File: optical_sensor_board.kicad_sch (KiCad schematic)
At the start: 33 parts, among them J2 Conn_01x09_Socket, U1 PMW3389DM‐T3QU, U3 LM317L_SOT-89

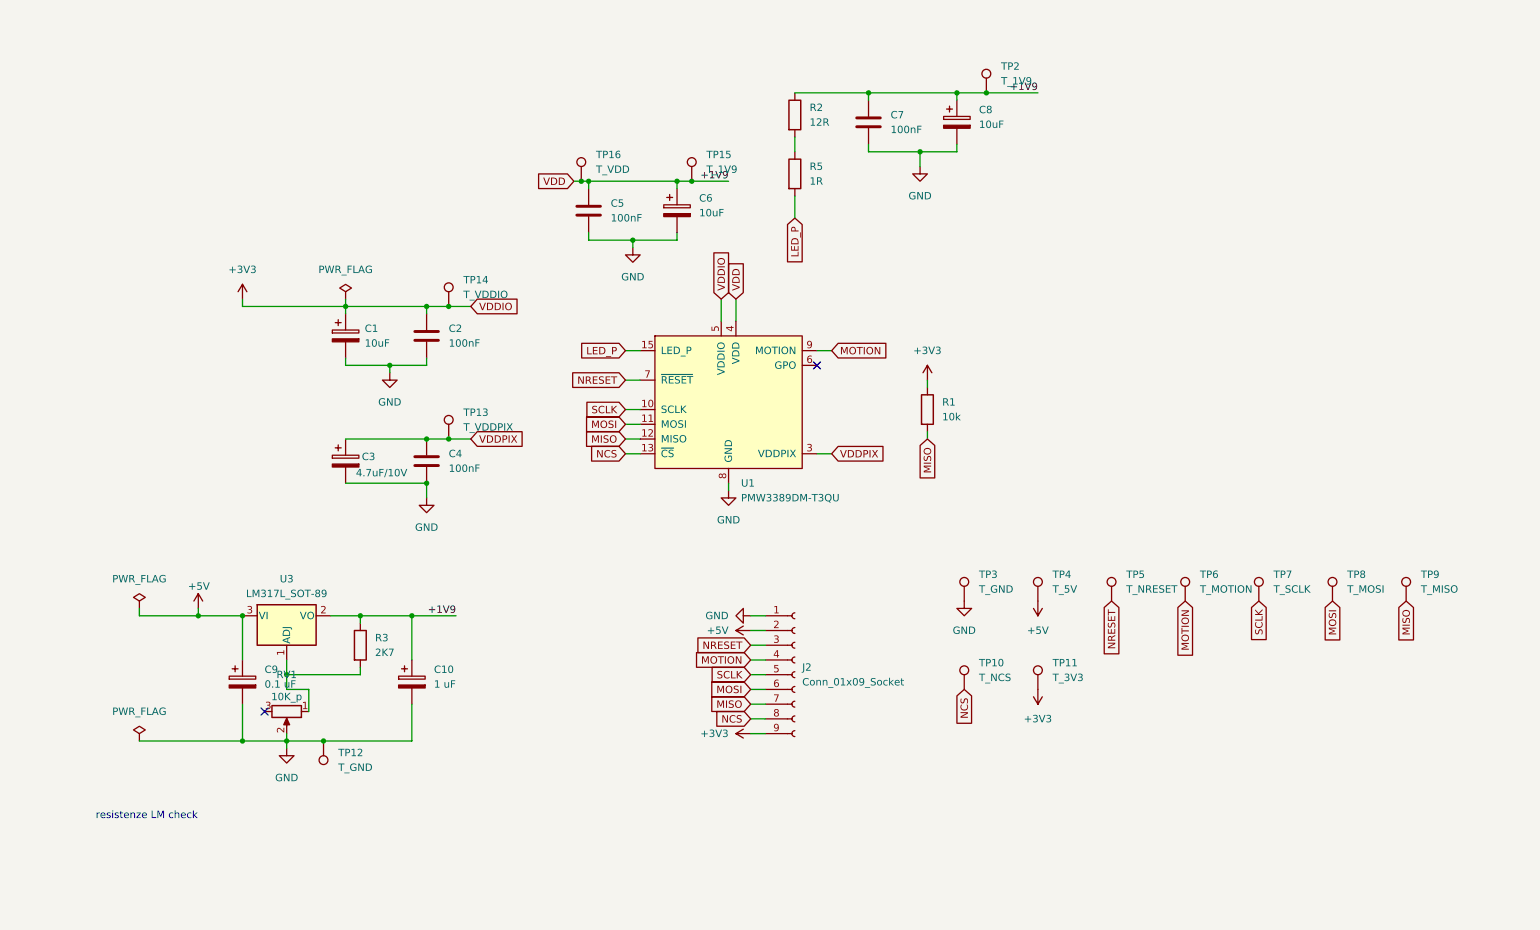
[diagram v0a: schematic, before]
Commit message: Modificato graficamente lo schematico + moidifiche al PCB
 - Sistemato graficamente lo schema
 - Corretto il testo del PCB
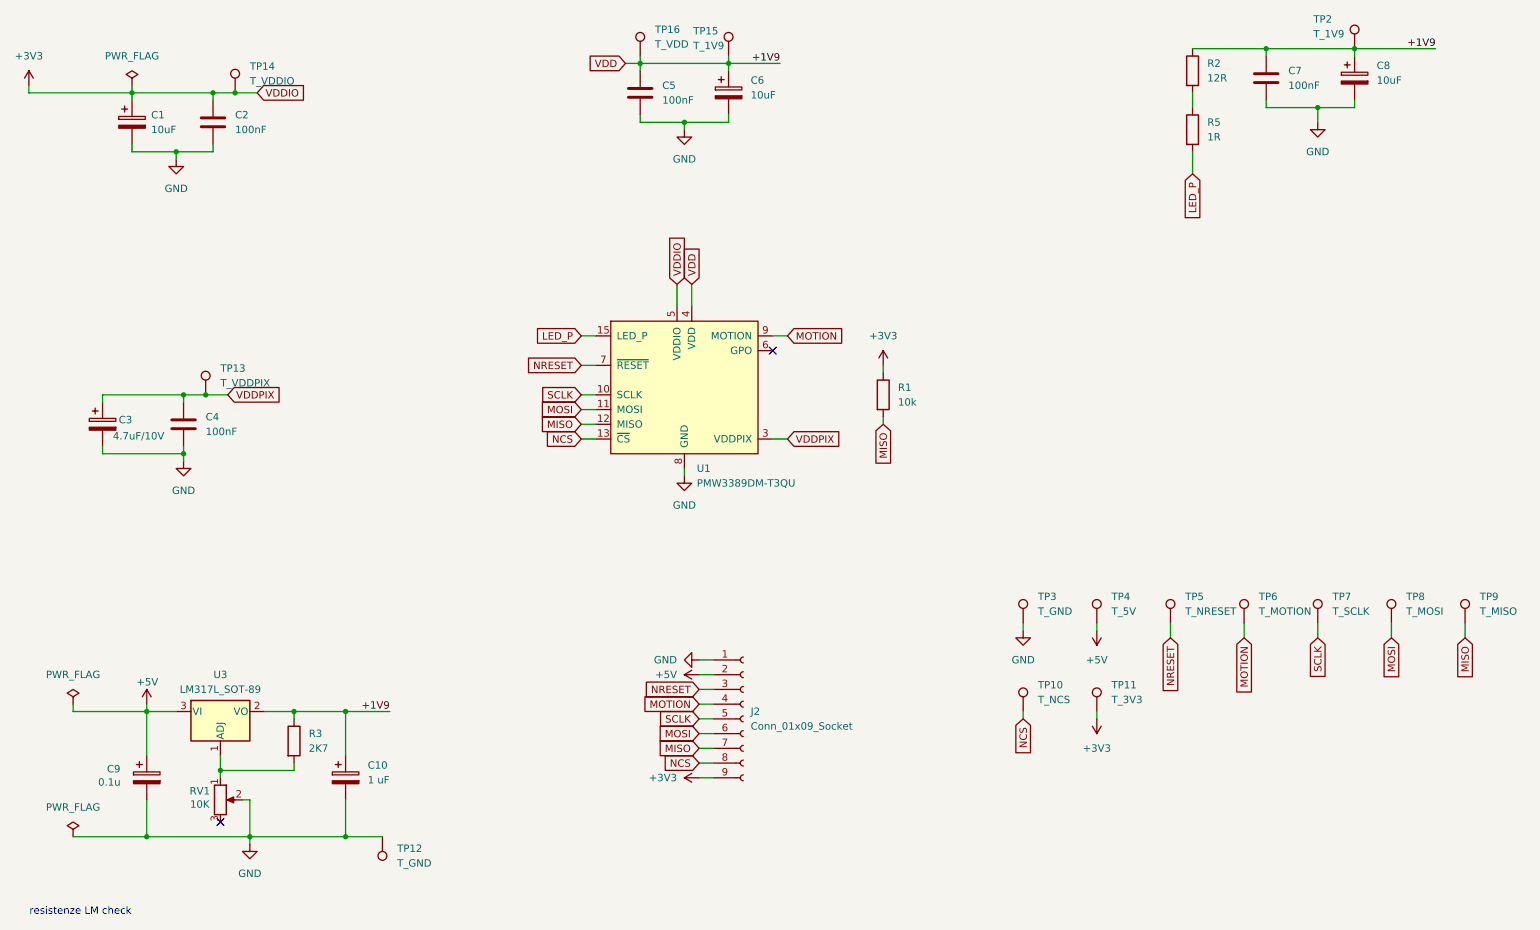
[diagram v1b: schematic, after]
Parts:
- C9: value 0.1 uF -> 0.1u
- RV1: value 10K_p -> 10K
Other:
- moved on the sheet: C1, C10, C2, C3, C4, C5, C6, C7, C8, C9, J2, R1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

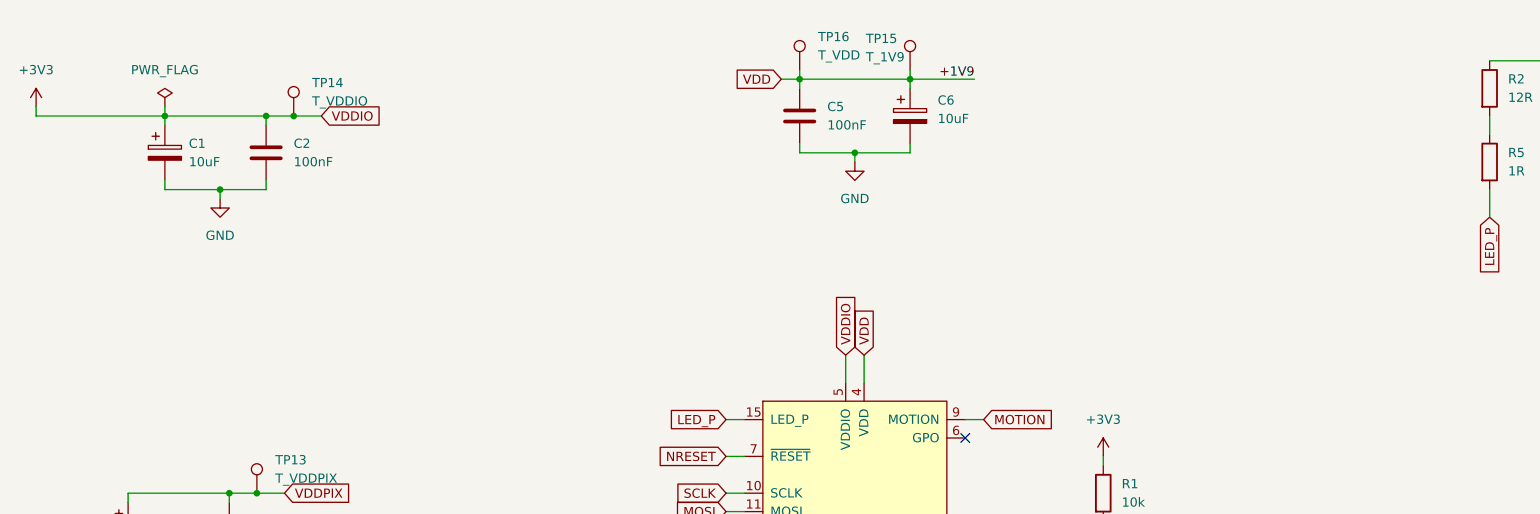
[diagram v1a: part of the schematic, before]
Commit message: Added a solder-jumer in series to the PS of the chip
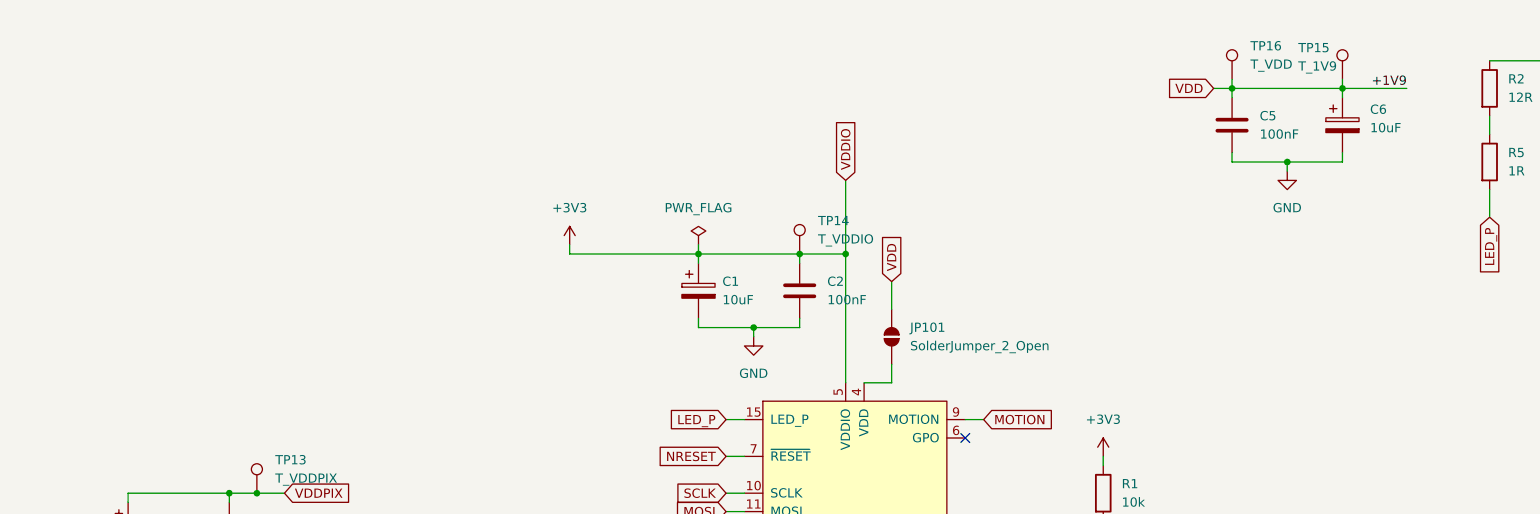
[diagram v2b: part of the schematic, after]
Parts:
- added JP101: SolderJumper_2_Open, Jumper:SolderJumper-2_P1.3mm_Open_TrianglePad1.0x1.5mm, symbol Jumper:SolderJumper_2_Open
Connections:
- net VDD: now also JP101.1 (A); no longer U1.4 (VDD)
- new net: JP101.2 (B), U1.4 (VDD)
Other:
- moved on the sheet: C1, C2, C5, C6, TP14, TP15, TP16

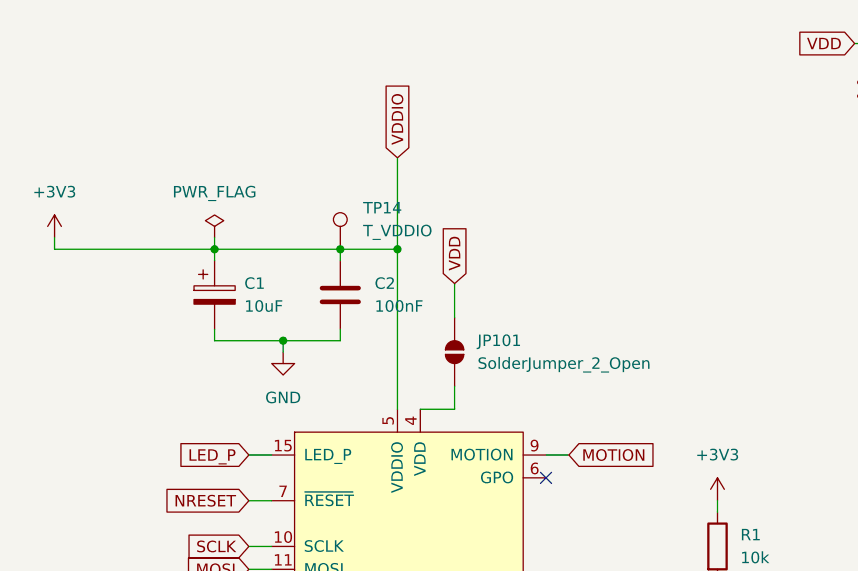
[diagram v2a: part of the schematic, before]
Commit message: Modified some traks of the PCB + exported new PDF for mastering
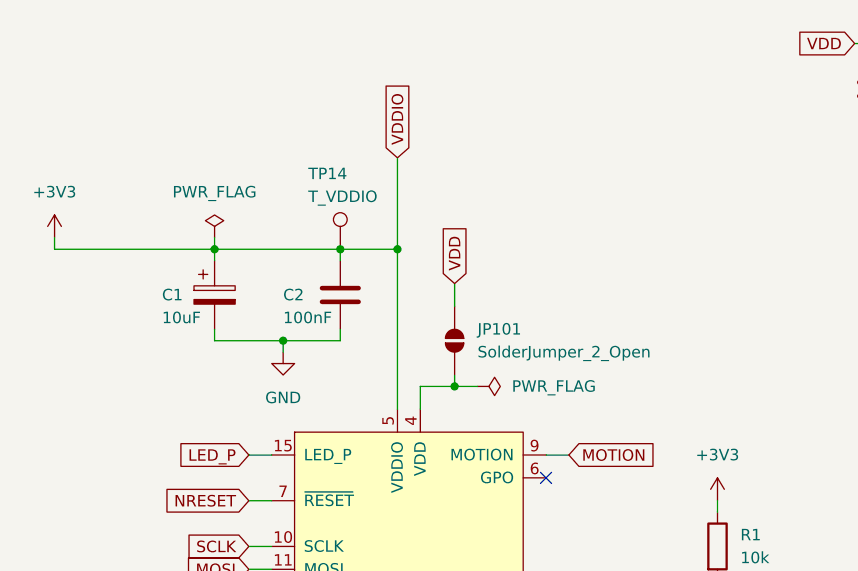
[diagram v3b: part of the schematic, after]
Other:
- moved on the sheet: JP101
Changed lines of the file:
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@@
 	)
 	(junction
+		(at 142.24 76.2)
+		(diameter 0)
+		(color 0 0 0 0)
+	)
+	(junction
 		(at 189.23 38.1)
 		(diameter 0)
@@
 	(wire
 		(pts
+			(xy 138.43 76.2) (xy 142.24 76.2)
+		)
+		(stroke
+			(width 0)
+			(type default)
+		)
+	)
+	(wire
+		(pts
 			(xy 50.8 95.25) (xy 50.8 93.98)
 		)
@@
 	(wire
 		(pts
-			(xy 142.24 64.77) (xy 142.24 68.58)
+			(xy 142.24 64.77) (xy 142.24 67.31)
 		)
 		(stroke
@@
 	(wire
 		(pts
-			(xy 142.24 78.74) (xy 138.43 78.74)
+			(xy 142.24 76.2) (xy 142.24 74.93)
 		)
 		(stroke
@@
 	(wire
 		(pts
-			(xy 142.24 76.2) (xy 142.24 78.74)
+			(xy 138.43 76.2) (xy 138.43 78.74)
 		)
 		(stroke
@@
 		)
 	)
+	(wire
+		(pts
+			(xy 144.78 76.2) (xy 142.24 76.2)
+		)
+		(stroke
+			(width 0)
+			(type default)
+		)
+	)
 	(label "+1V9"
 		(at 266.7 34.29 180)
@@
 		(on_board yes)
 		(dnp no)
-		(fields_autoplaced yes)
 		(property "Reference" "TP14"
-			(at 132.08 56.3879 0)
+			(at 125.984 52.578 0)
 			(effects
 				(font
@@
 		)
 		(property "Value" "T_VDDIO"
-			(at 132.08 58.9279 0)
+			(at 125.984 55.118 0)
 			(effects
 				(font
@@
 		(on_board yes)
 		(dnp no)
-		(fields_autoplaced yes)
 		(property "Reference" "C2"
-			(at 133.35 64.7699 0)
+			(at 123.19 66.04 0)
 			(effects
 				(font
@@
 		)
 		(property "Value" "100nF"
-			(at 133.35 67.3099 0)
+			(at 123.19 68.58 0)
 			(effects
 				(font
@@
 		(dnp no)
 		(property "Reference" "C1"
-			(at 118.872 64.77 0)
+			(at 109.728 66.04 0)
 			(effects
 				(font
@@
 		)
 		(property "Value" "10uF"
-			(at 118.872 67.31 0)
+			(at 109.728 68.58 0)
 			(effects
 				(font
@@
 	)
 	(symbol
+		(lib_id "power:PWR_FLAG")
+		(at 144.78 76.2 270)
+		(unit 1)
+		(exclude_from_sim no)
+		(in_bom yes)
+		(on_board yes)
+		(dnp no)
+		(fields_autoplaced yes)
+		(property "Reference" "#FLG0103"
+			(at 146.685 76.2 0)
+			(effects
+				(font
+					(size 1.27 1.27)
+				)
+				(hide yes)
+			)
+		)
+		(property "Value" "PWR_FLAG"
+			(at 148.59 76.1999 90)
+			(effects
+				(font
+					(size 1.27 1.27)
+				)
+				(justify left)
+			)
+		)
+		(property "Footprint" ""
+			(at 144.78 76.2 0)
+			(effects
+				(font
+					(size 1.27 1.27)
+				)
+				(hide yes)
+			)
+		)
+		(property "Datasheet" "~"
+			(at 144.78 76.2 0)
+			(effects
+				(font
+					(size 1.27 1.27)
+				)
+				(hide yes)
+			)
+		)
+		(property "Description" "Special symbol for telling ERC where power comes from"
+			(at 144.78 76.2 0)
+			(effects
+				(font
+					(size 1.27 1.27)
+				)
+				(hide yes)
+			)
+		)
+		(pin "1"
+		)
+		(instances
+			(project "optical_sensor_board"
+				(path "/bc898632-37cb-47d1-8655-c4a22efc7ca2"
+					(reference "#FLG0103")
+					(unit 1)
+				)
+			)
+		)
+	)
+	(symbol
 		(lib_id "Device:R")
 		(at 69.85 153.67 0)
@@
 	(symbol
 		(lib_id "Jumper:SolderJumper_2_Open")
-		(at 142.24 72.39 270)
+		(at 142.24 71.12 270)
 		(unit 1)
 		(exclude_from_sim no)
@@
 		(fields_autoplaced yes)
 		(property "Reference" "JP101"
-			(at 144.78 71.1199 90)
+			(at 144.78 69.8499 90)
 			(effects
 				(font
@@
 		)
 		(property "Value" "SolderJumper_2_Open"
-			(at 144.78 73.6599 90)
+			(at 144.78 72.3899 90)
 			(effects
 				(font
@@
 		)
 		(property "Footprint" "Jumper:SolderJumper-2_P1.3mm_Open_TrianglePad1.0x1.5mm"
-			(at 142.24 72.39 0)
+			(at 142.24 71.12 0)
 			(effects
 				(font
@@
 		)
 		(property "Datasheet" "~"
-			(at 142.24 72.39 0)
+			(at 142.24 71.12 0)
 			(effects
 				(font
@@
 		)
 		(property "Description" "Solder Jumper, 2-pole, open"
-			(at 142.24 72.39 0)
+			(at 142.24 71.12 0)
 			(effects
 				(font
